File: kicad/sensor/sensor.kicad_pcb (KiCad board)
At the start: 2 copper layers, 80 x 30 mm, 49 parts, among them J1 TE_1116503-1, U1 LP2985A-10DBVx, U2 LMH6553MR/NOPB

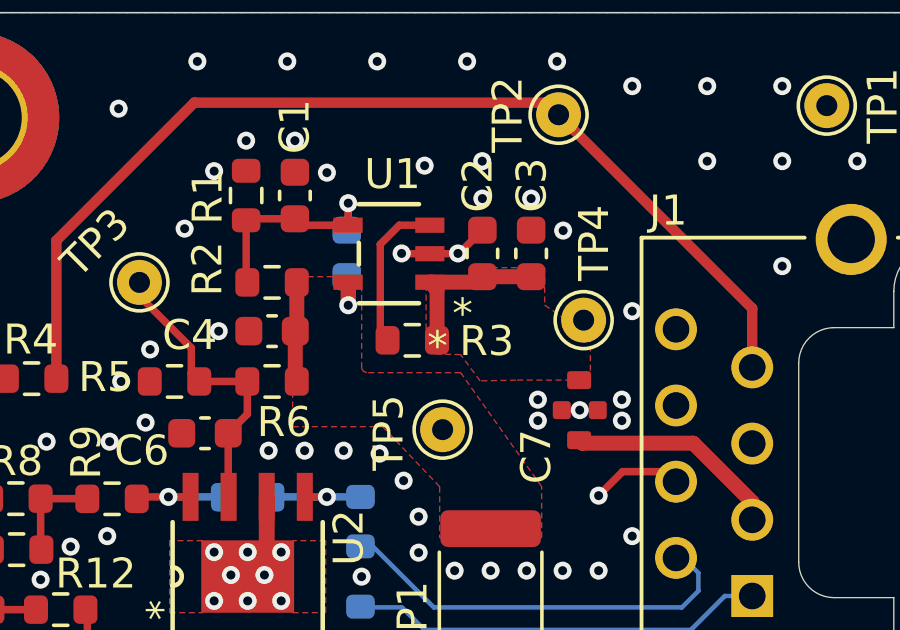
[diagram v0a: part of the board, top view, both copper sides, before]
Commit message: Properly exclude tolerated DRC errors and fix silkscreen overlap
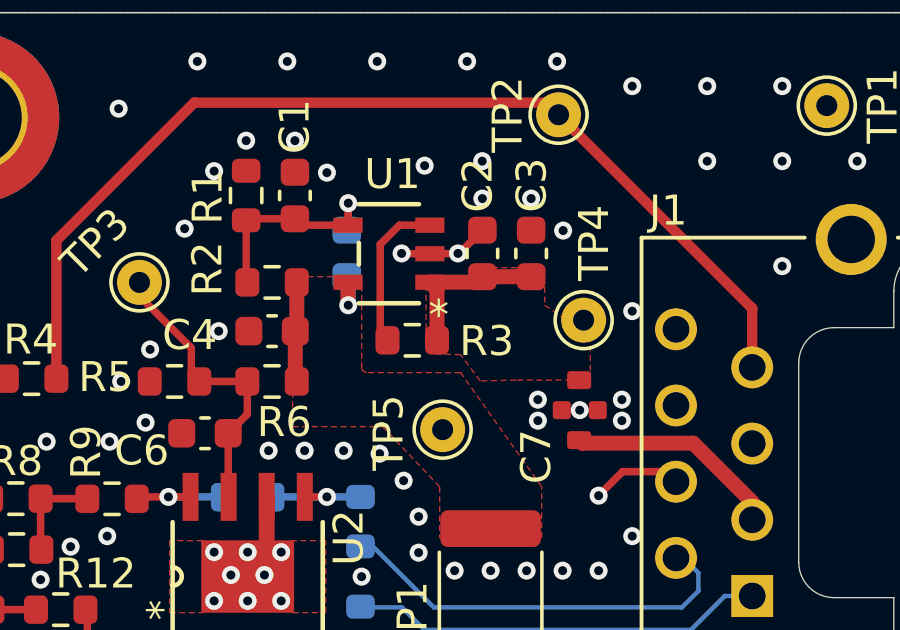
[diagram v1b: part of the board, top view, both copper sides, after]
